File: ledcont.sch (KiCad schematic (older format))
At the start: 21 parts, among them J1 Screw_Terminal_01x02, J2 Screw_Terminal_01x02, Q1 ?, SW1 SW_SPST, U1 PAM2804

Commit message: Updated to the latest and greatest.
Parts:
- removed C?: 10uF, symbol Device:C
- removed D1, D2: TL431, symbol ledcont:TL431
- removed D3: LED, symbol Device:LED_Series
- removed Q1: ?, symbol Device:Q_PMOS_DGS
- removed R4: 1k, symbol Device:R
- removed R5: ?, symbol Device:R
- removed RV1: 5k, symbol Device:R_POT_TRIM
- removed RV2: ?, symbol Device:R_POT
- removed SW1: SW_SPST, symbol Switch:SW_SPST
- added C3: 10uF, Capacitor_SMD:C_1206_3216Metric, symbol Device:C
- added C4: 1uF, Capacitor_SMD:C_1206_3216Metric, symbol Device:C
- added C5, C6: .1uF, Capacitor_SMD:C_1206_3216Metric, symbol Device:C
- added D1: D_Schottky, symbol Device:D_Schottky
- added R10: 10k, Resistor_SMD:R_1206_3216Metric, symbol Device:R
- added R6: 1k, Resistor_SMD:R_1206_3216Metric, symbol Device:R
- added R7: 20k, Resistor_SMD:R_1206_3216Metric, symbol Device:R
- added R9: 9k, Resistor_SMD:R_1206_3216Metric, symbol Device:R
- added RV1: SPST, symbol ledcont:R_POT_SPST
- added U2: TSM102A, Package_SO:SOIC-16_3.9x9.9mm_P1.27mm, symbol Power_Management:TSM102A
- C1, C2: footprint (none) -> Capacitor_SMD:C_1206_3216Metric
- R1: value 10k -> 1k; footprint (none) -> Resistor_SMD:R_1206_3216Metric
- R2: value 1k -> 2k; footprint (none) -> Resistor_SMD:R_1206_3216Metric
- R3: footprint (none) -> Resistor_SMD:R_1206_3216Metric
- R4: renamed from R6; footprint (none) -> Resistor_SMD:R_1206_3216Metric
- R5: renamed from R7; footprint (none) -> Resistor_SMD:R_1206_3216Metric
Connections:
- net GND: now also R3.1, C3.2, C4.2, C5.2, C6.2, R10.2, RV1.1, RV1.2 (B), U2.13 (V-), U2.14 (+); no longer R1.2, R3.2
- net at R4.1, U1.5 (FB): now also R9.2
- net at C1.1, U1.4 (VIN): now also C3.1, C4.1, C5.1, D1.1 (K), RV1.5
- net at U1.1 (EN): now also R10.1, R6.2, U2.1; no longer R3.1
- net at R2.1: now also R3.2, U2.8
- net Vref: now reaches R1.1
- net Vref: now also R2.2, R7.1, U2.15 (-), U2.2 (-), U2.9
- net +BATT: no longer names the net of J1.1 (Pin_1)
- net +BATT: now also D1.2 (A); no longer R2.2
- new net: R7.2, RV1.3, U2.12 (+), U2.5 (+)
- new net: C6.1, R1.2, R6.1, RV1.4, U2.3 (+), U2.4 (V+)
- new net: R9.1, U2.6 (-), U2.7
- new net: U2.10 (-), U2.11
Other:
- note added: "18650 Battery"
- note added: "Unused"
- note added: "XXX -\nLet's always drive the output low? Is this right?"
- moved on the sheet: C1, C2, J1, J2, L1, R4, R5, U1

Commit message: Assigned footprints.
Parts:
- C1, C2, C3, C4, C5, C6: footprint Capacitor_SMD:C_1206_3216Metric -> Capacitor_SMD:C_1206_3216Metric_Pad1.42x1.75mm_HandSolder
- D1: footprint (none) -> Diode_SMD:D_1206_3216Metric_Pad1.42x1.75mm_HandSolder
- J1, J2: footprint (none) -> TerminalBlock_Phoenix:TerminalBlock_Phoenix_PT-1,5-2-3.5-H_1x02_P3.50mm_Horizontal
- L1: footprint (none) -> Inductor_SMD:L_1812_4532Metric_Pad1.30x3.40mm_HandSolder
- R1, R10, R2, R3, R4, R5, R6, R7, R9: footprint Resistor_SMD:R_1206_3216Metric -> Resistor_SMD:R_1206_3216Metric_Pad1.42x1.75mm_HandSolder
- RV1: footprint (none) -> ledcont:P091_S
- U1: footprint (none) -> ledcont:TSOT25
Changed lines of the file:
@@
 F 0 "R4" V 8107 3050 50  0000 C CNN
 F 1 "1k" V 8016 3050 50  0000 C CNN
-F 2 "Resistor_SMD:R_1206_3216Metric" V 7830 3050 50  0001 C CNN
+F 2 "Resistor_SMD:R_1206_3216Metric_Pad1.42x1.75mm_HandSolder" V 7830 3050 50  0001 C CNN
 F 3 "~" H 7900 3050 50  0001 C CNN
 	1    7900 3050
@@
 F 0 "R5" H 8630 3346 50  0000 R CNN
 F 1 "0.214" H 8630 3255 50  0000 R CNN
-F 2 "Resistor_SMD:R_1206_3216Metric" V 8630 3300 50  0001 C CNN
+F 2 "Resistor_SMD:R_1206_3216Metric_Pad1.42x1.75mm_HandSolder" V 8630 3300 50  0001 C CNN
 F 3 "~" H 8700 3300 50  0001 C CNN
 	1    8700 3300
@@
 F 0 "C2" H 8265 2396 50  0000 L CNN
 F 1 "10uF" H 8265 2305 50  0000 L CNN
-F 2 "Capacitor_SMD:C_1206_3216Metric" H 8188 2200 50  0001 C CNN
+F 2 "Capacitor_SMD:C_1206_3216Metric_Pad1.42x1.75mm_HandSolder" H 8188 2200 50  0001 C CNN
 F 3 "~" H 8150 2350 50  0001 C CNN
 	1    8150 2350
@@
 F 0 "L1" V 8040 2100 50  0000 C CNN
 F 1 "4.7uH" V 7949 2100 50  0000 C CNN
-F 2 "" H 7850 2100 50  0001 C CNN
+F 2 "Inductor_SMD:L_1812_4532Metric_Pad1.30x3.40mm_HandSolder" H 7850 2100 50  0001 C CNN
 F 3 "~" H 7850 2100 50  0001 C CNN
 	1    7850 2100
@@
 F 0 "U1" H 6550 2665 50  0000 C CNN
 F 1 "PAM2804" H 6550 2574 50  0000 C CNN
-F 2 "" H 6550 2250 50  0001 C CNN
+F 2 "ledcont:TSOT25" H 6550 2250 50  0001 C CNN
 F 3 "" H 6550 2250 50  0001 C CNN
 	1    6550 2250
@@
 F 0 "C1" H 5786 2396 50  0000 R CNN
 F 1 "10uF" H 5786 2305 50  0000 R CNN
-F 2 "Capacitor_SMD:C_1206_3216Metric" H 5938 2200 50  0001 C CNN
+F 2 "Capacitor_SMD:C_1206_3216Metric_Pad1.42x1.75mm_HandSolder" H 5938 2200 50  0001 C CNN
 F 3 "~" H 5900 2350 50  0001 C CNN
 	1    5900 2350
@@
 F 0 "J2" H 8980 2046 50  0000 L CNN
 F 1 "Screw_Terminal_01x02" H 8980 2001 50  0001 L CNN
-F 2 "" H 8900 2100 50  0001 C CNN
+F 2 "TerminalBlock_Phoenix:TerminalBlock_Phoenix_PT-1,5-2-3.5-H_1x02_P3.50mm_Horizontal" H 8900 2100 50  0001 C CNN
 F 3 "~" H 8900 2100 50  0001 C CNN
 	1    8900 2100
@@
 F 0 "J1" H 2670 2225 50  0000 C CNN
 F 1 "Screw_Terminal_01x02" H 2670 2226 50  0001 C CNN
-F 2 "" H 2750 2100 50  0001 C CNN
+F 2 "TerminalBlock_Phoenix:TerminalBlock_Phoenix_PT-1,5-2-3.5-H_1x02_P3.50mm_Horizontal" H 2750 2100 50  0001 C CNN
 F 3 "~" H 2750 2100 50  0001 C CNN
 	1    2750 2100
@@
 F 0 "RV1" H 6680 4246 50  0000 R CNN
 F 1 "SPST" H 6680 4155 50  0000 R CNN
-F 2 "" H 6750 4200 50  0001 C CNN
+F 2 "ledcont:P091_S" H 6750 4200 50  0001 C CNN
 F 3 "~" H 6750 4200 50  0001 C CNN
 	1    6750 4200
@@
 F 0 "RV1" H 5088 2396 50  0000 L CNN
 F 1 "SPST" H 5088 2305 50  0001 L CNN
-F 2 "" H 4950 2350 50  0001 C CNN
+F 2 "ledcont:P091_S" H 4950 2350 50  0001 C CNN
 F 3 "~" H 4950 2350 50  0001 C CNN
 	2    4950 2350
@@
 F 0 "R1" V 4243 3500 50  0000 C CNN
 F 1 "1k" V 4334 3500 50  0000 C CNN
-F 2 "Resistor_SMD:R_1206_3216Metric" V 4380 3500 50  0001 C CNN
+F 2 "Resistor_SMD:R_1206_3216Metric_Pad1.42x1.75mm_HandSolder" V 4380 3500 50  0001 C CNN
 F 3 "~" H 4450 3500 50  0001 C CNN
 	1    4450 3500
@@
 F 0 "R2" H 4130 4104 50  0000 R CNN
 F 1 "2k" H 4130 4195 50  0000 R CNN
-F 2 "Resistor_SMD:R_1206_3216Metric" V 4130 4150 50  0001 C CNN
+F 2 "Resistor_SMD:R_1206_3216Metric_Pad1.42x1.75mm_HandSolder" V 4130 4150 50  0001 C CNN
 F 3 "~" H 4200 4150 50  0001 C CNN
 	1    4200 4150
@@
 F 0 "R3" H 4130 4504 50  0000 R CNN
 F 1 "10k" H 4130 4595 50  0000 R CNN
-F 2 "Resistor_SMD:R_1206_3216Metric" V 4130 4550 50  0001 C CNN
+F 2 "Resistor_SMD:R_1206_3216Metric_Pad1.42x1.75mm_HandSolder" V 4130 4550 50  0001 C CNN
 F 3 "~" H 4200 4550 50  0001 C CNN
 	1    4200 4550
@@
 F 0 "R6" V 5757 3050 50  0000 C CNN
 F 1 "1k" V 5666 3050 50  0000 C CNN
-F 2 "Resistor_SMD:R_1206_3216Metric" V 5480 3050 50  0001 C CNN
+F 2 "Resistor_SMD:R_1206_3216Metric_Pad1.42x1.75mm_HandSolder" V 5480 3050 50  0001 C CNN
 F 3 "~" H 5550 3050 50  0001 C CNN
 	1    5550 3050
@@
 F 0 "R7" H 6820 3846 50  0000 L CNN
 F 1 "20k" H 6820 3755 50  0000 L CNN
-F 2 "Resistor_SMD:R_1206_3216Metric" V 6680 3800 50  0001 C CNN
+F 2 "Resistor_SMD:R_1206_3216Metric_Pad1.42x1.75mm_HandSolder" V 6680 3800 50  0001 C CNN
 F 3 "~" H 6750 3800 50  0001 C CNN
 	1    6750 3800
@@
 F 0 "R9" V 7607 3050 50  0000 C CNN
 F 1 "9k" V 7516 3050 50  0000 C CNN
-F 2 "Resistor_SMD:R_1206_3216Metric" V 7330 3050 50  0001 C CNN
+F 2 "Resistor_SMD:R_1206_3216Metric_Pad1.42x1.75mm_HandSolder" V 7330 3050 50  0001 C CNN
 F 3 "~" H 7400 3050 50  0001 C CNN
 	1    7400 3050
@@
 F 0 "D1" H 3400 1884 50  0000 C CNN
 F 1 "D_Schottky" H 3400 1975 50  0000 C CNN
-F 2 "" H 3400 2100 50  0001 C CNN
+F 2 "Diode_SMD:D_1206_3216Metric_Pad1.42x1.75mm_HandSolder" H 3400 2100 50  0001 C CNN
 F 3 "~" H 3400 2100 50  0001 C CNN
 	1    3400 2100
@@
 F 0 "C3" H 3636 2296 50  0000 R CNN
 F 1 "10uF" H 3636 2205 50  0000 R CNN
-F 2 "Capacitor_SMD:C_1206_3216Metric" H 3788 2100 50  0001 C CNN
+F 2 "Capacitor_SMD:C_1206_3216Metric_Pad1.42x1.75mm_HandSolder" H 3788 2100 50  0001 C CNN
 F 3 "~" H 3750 2250 50  0001 C CNN
 	1    3750 2250
@@
 F 0 "C4" H 4036 2296 50  0000 R CNN
 F 1 "1uF" H 4036 2205 50  0000 R CNN
-F 2 "Capacitor_SMD:C_1206_3216Metric" H 4188 2100 50  0001 C CNN
+F 2 "Capacitor_SMD:C_1206_3216Metric_Pad1.42x1.75mm_HandSolder" H 4188 2100 50  0001 C CNN
 F 3 "~" H 4150 2250 50  0001 C CNN
 	1    4150 2250
@@
 F 0 "C5" H 4486 2296 50  0000 R CNN
 F 1 ".1uF" H 4486 2205 50  0000 R CNN
-F 2 "Capacitor_SMD:C_1206_3216Metric" H 4638 2100 50  0001 C CNN
+F 2 "Capacitor_SMD:C_1206_3216Metric_Pad1.42x1.75mm_HandSolder" H 4638 2100 50  0001 C CNN
 F 3 "~" H 4600 2250 50  0001 C CNN
 	1    4600 2250
@@
 F 0 "R10" H 6170 3646 50  0000 L CNN
 F 1 "10k" H 6170 3555 50  0000 L CNN
-F 2 "Resistor_SMD:R_1206_3216Metric" V 6030 3600 50  0001 C CNN
+F 2 "Resistor_SMD:R_1206_3216Metric_Pad1.42x1.75mm_HandSolder" V 6030 3600 50  0001 C CNN
 F 3 "~" H 6100 3600 50  0001 C CNN
 	1    6100 3600
@@
 F 0 "C6" H 5065 3996 50  0000 L CNN
 F 1 ".1uF" H 5065 3905 50  0000 L CNN
-F 2 "Capacitor_SMD:C_1206_3216Metric" H 4988 3800 50  0001 C CNN
+F 2 "Capacitor_SMD:C_1206_3216Metric_Pad1.42x1.75mm_HandSolder" H 4988 3800 50  0001 C CNN
 F 3 "~" H 4950 3950 50  0001 C CNN
 	1    4950 3950

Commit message: More progress.
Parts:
- C1: renamed from C3; Part (none) -> CL31B106KOHNFNE
- C2: renamed from C4; Part (none) -> CL31B105MAHNNNE
- C3: renamed from C5; Part (none) -> CL31B104KBCNNNC
- C4: renamed from C6; Part (none) -> CL31B104KBCNNNC
- C5: renamed from C1; Part (none) -> CL31B106KOHNFNE
- C6: renamed from C2; Part (none) -> CL31B106KOHNFNE
- D1: footprint Diode_SMD:D_1206_3216Metric_Pad1.42x1.75mm_HandSolder -> Diode_SMD:D_SOD-123F; Part (none) -> NRVTS245ESFT1G
- J1, J2: Part (none) -> 1984617
- L1: Part (none) -> LQH43PN4R7M26L
- R1: renamed from R2; Part (none) -> RC1206FR-072KL; Tolerance (none) -> 1%
- R2: renamed from R3; Part (none) -> RC1206FR-0710KL; Tolerance (none) -> 1%
- R3: renamed from R1; Part (none) -> RC1206FR-071KL; Tolerance (none) -> 1%
- R4: renamed from R6; Part (none) -> RC1206FR-071KL; Tolerance (none) -> 1%
- R5: renamed from R10; Part (none) -> RC1206FR-0710KL; Tolerance (none) -> 1%
- R6: renamed from R7; Part (none) -> RC1206FR-0720KL
- R7: renamed from R9; Part (none) -> RC1206FR-079K09L; Tolerance (none) -> 1%
- R8: renamed from R4; Part (none) -> RC1206FR-071KL; Tolerance (none) -> 1%
- R9: renamed from R5; value 0.214 -> 0.200; Part (none) -> PT1206FR-070R2L; Tolerance (none) -> 1%
- RV1: Part (none) -> P091S-FC20BR10K
- U1: Part (none) -> PAM2804AAB010
- U2: Part (none) -> TSM102AIDT

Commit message: Checkpoint before real board layout.
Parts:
- RV1: value SPST -> 10k
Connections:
- net GND: now also RV1.3; no longer RV1.1
- net at R6.2, U2.12 (+), U2.5 (+): now also RV1.1; no longer RV1.3
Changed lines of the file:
@@
 U 1 1 5C458CC6
 P 6750 4200
-F 0 "RV1" H 6680 4246 50  0000 R CNN
-F 1 "SPST" H 6680 4155 50  0000 R CNN
+F 0 "RV1" H 6680 4154 50  0000 R CNN
+F 1 "10k" H 6680 4245 50  0000 R CNN
 F 2 "ledcont:P091_S" H 6750 4200 50  0001 C CNN
 F 3 "~" H 6750 4200 50  0001 C CNN
 F 4 "P091S-FC20BR10K" H 0   0   50  0001 C CNN "Part"
 	1    6750 4200
-	-1   0    0    -1
+	-1   0    0    1
 $EndComp
 $Comp

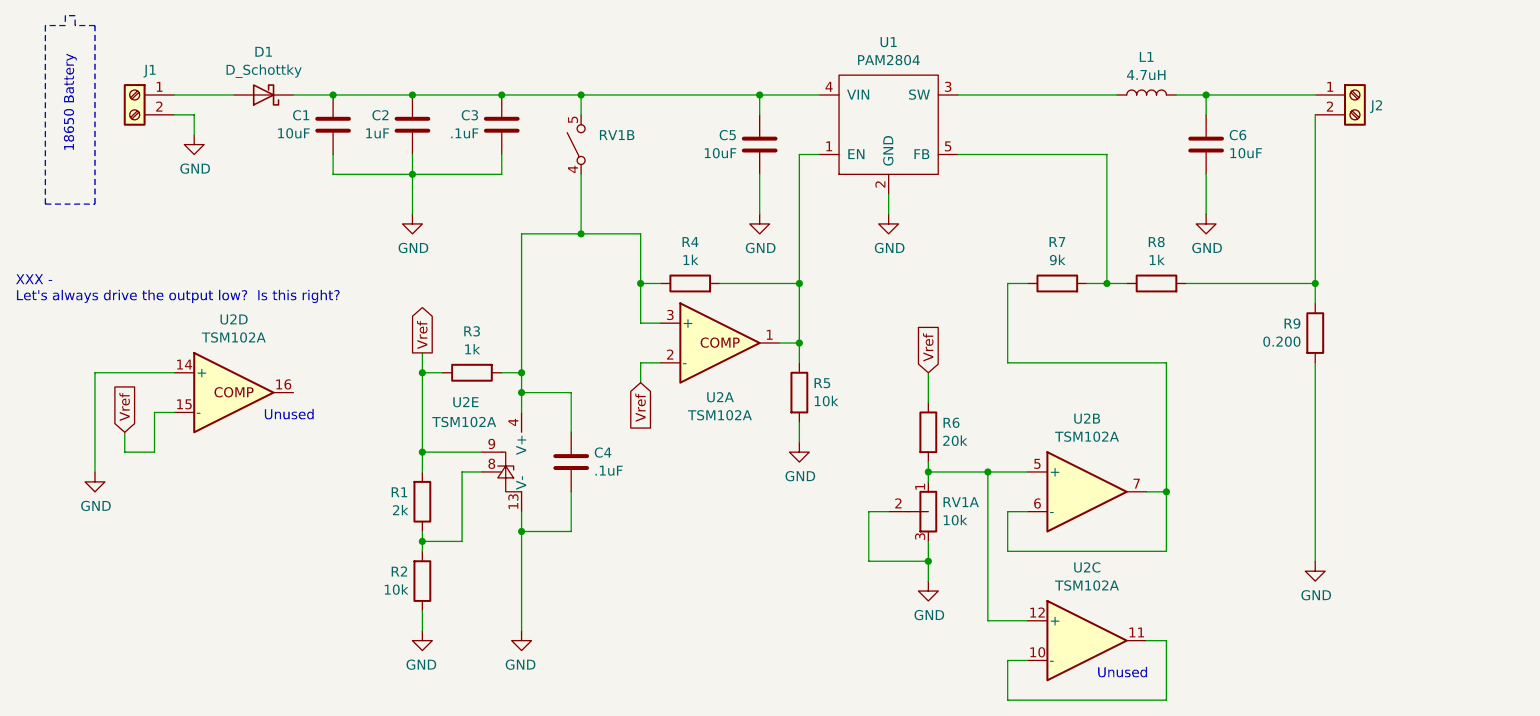
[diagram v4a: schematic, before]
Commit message: Finished first attempt at board layout.
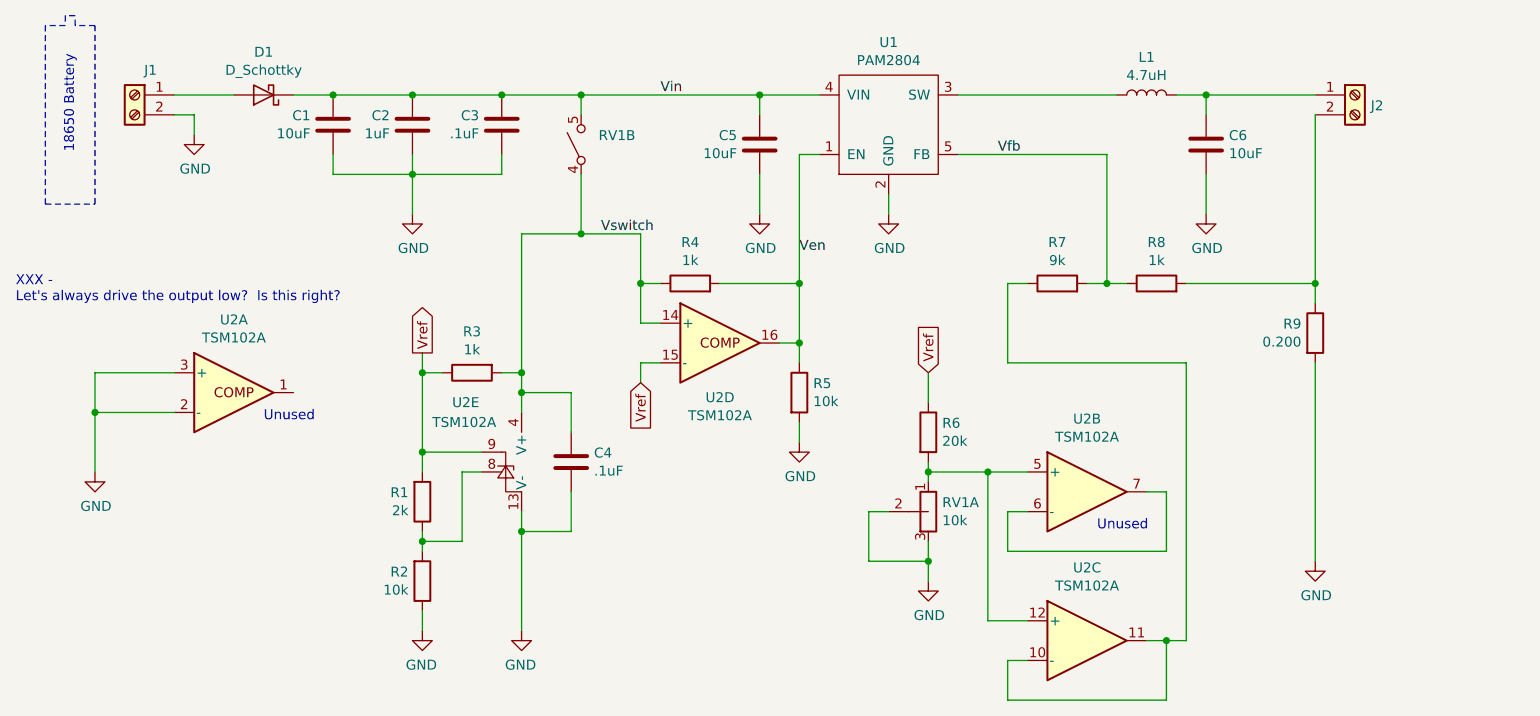
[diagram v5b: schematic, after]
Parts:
- RV1: value SPST -> 10k
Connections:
- net GND: now also U2.2 (-), U2.3 (+); no longer U2.14 (+)
- net Vref: now also U2.15 (-); no longer U2.15 (-), U2.2 (-)
- net Vfb: now reaches R7.2, R8.1, U1.5 (FB)
- net Vin: now reaches C1.1, C2.1, C3.1, C5.1, D1.1 (K), RV1.5, U1.4 (VIN)
- net Vswitch: now reaches C4.1, R3.2, R4.1, RV1.4, U2.4 (V+)
- net Vswitch: now also U2.14 (+); no longer U2.3 (+)
- net Ven: now reaches R4.2, R5.1, U1.1 (EN)
- net Ven: now also U2.16; no longer U2.1
- net at U2.6 (-), U2.7: no longer R7.1
- net at U2.10 (-), U2.11: now also R7.1
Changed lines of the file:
@@
 P 4950 2350
 F 0 "RV1" H 5088 2396 50  0000 L CNN
-F 1 "SPST" H 5088 2305 50  0001 L CNN
+F 1 "10k" H 5088 2305 50  0001 L CNN
 F 2 "ledcont:P091_S" H 4950 2350 50  0001 C CNN
 F 3 "~" H 4950 2350 50  0001 C CNN
@@
 $Comp
 L Power_Management:TSM102A U2
-U 1 1 5C4640C2
+U 4 1 5C4640C2
 P 5700 3350
 F 0 "U2" H 5700 3075 50  0000 C CNN
@@
 F 3 "http://www.st.com/resource/en/datasheet/tsm102.pdf" H 5750 3550 50  0001 C CNN
 F 4 "TSM102AIDT" H 0   0   50  0001 C CNN "Part"
-	1    5700 3350
+	4    5700 3350
 	1    0    0    -1
 $EndComp
@@
 Wire Wire Line
 	7150 4200 7150 4400
-Wire Wire Line
-	7150 4400 7950 4400
-Wire Wire Line
-	7950 4400 7950 4100
 $Comp
 L Device:R R7
@@
 Wire Wire Line
 	7950 4850 7850 4850
-Text Notes 7600 5050 0    50   ~ 0
+Text Notes 7600 4300 0    50   ~ 0
 Unused
 Text Notes 3400 3750 0    50   ~ 0
@@
 $Comp
 L Power_Management:TSM102A U2
-U 4 1 5C4AD8B0
+U 1 1 5C4AD8B0
 P 3250 3600
 F 0 "U2" H 3250 3967 50  0000 C CNN
@@
 F 3 "http://www.st.com/resource/en/datasheet/tsm102.pdf" H 3300 3800 50  0001 C CNN
 F 4 "TSM102AIDT" H 0   0   50  0001 C CNN "Part"
-	4    3250 3600
+	1    3250 3600
 	1    0    0    -1
 $EndComp
 Wire Wire Line
 	2950 3500 2550 3500
-Text GLabel 2700 3800 1    50   Input ~ 0
-Vref
-Wire Wire Line
-	2550 3500 2550 4000
-Wire Wire Line
-	2850 3900 2700 3900
-Wire Wire Line
-	2700 3900 2700 3800
-Wire Wire Line
-	2950 3700 2850 3700
-Wire Wire Line
-	2850 3700 2850 3900
+Wire Wire Line
+	2550 3500 2550 3700
 Text Notes 2150 3150 0    50   ~ 0
 XXX -\nLet's always drive the output low?  Is this right?
@@
 	6100 3750 6100 3850
 Connection ~ 7050 4000
-Connection ~ 7950 4100
 Wire Wire Line
 	7950 4100 7850 4100
@@
 Wire Wire Line
 	7150 3050 7150 3450
-Wire Wire Line
-	7150 3450 7950 3450
-Wire Wire Line
-	7950 3450 7950 4100
 Text GLabel 5300 3550 3    50   Input ~ 0
 Vref
@@
 	1    0    0    -1
 $EndComp
+Text Label 5100 2800 0    50   ~ 0
+Vswitch
+Text Label 5400 2100 0    50   ~ 0
+Vin
+Text Label 7100 2400 0    50   ~ 0
+Vfb
+Wire Wire Line
+	7150 4400 7950 4400
+Wire Wire Line
+	7950 4100 7950 4400
+Wire Wire Line
+	8050 3450 8050 4850
+Wire Wire Line
+	8050 4850 7950 4850
+Wire Wire Line
+	7150 3450 8050 3450
+Connection ~ 7950 4850
+Text Label 6100 2900 0    50   ~ 0
+Ven
+Wire Wire Line
+	2950 3700 2550 3700
+Connection ~ 2550 3700
+Wire Wire Line
+	2550 3700 2550 4000
 $EndSCHEMATC

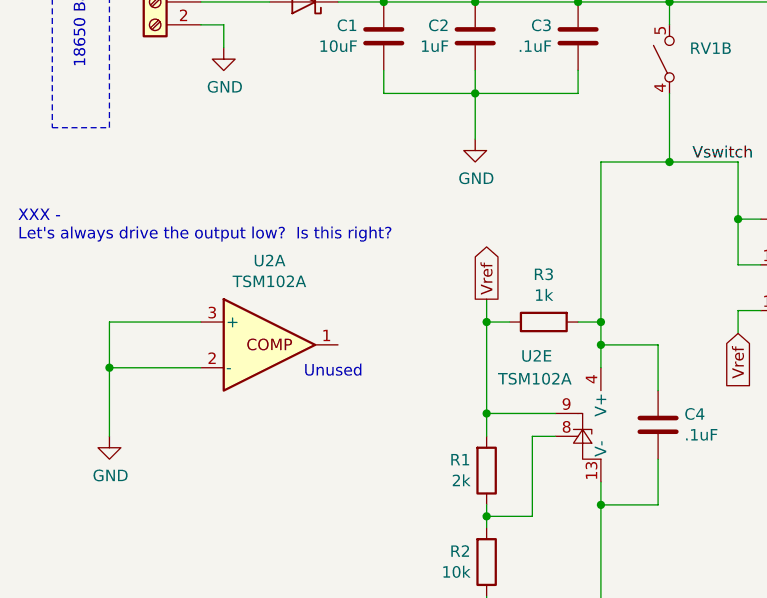
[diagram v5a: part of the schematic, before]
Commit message: Board cutout.  Rewired unused comparator.
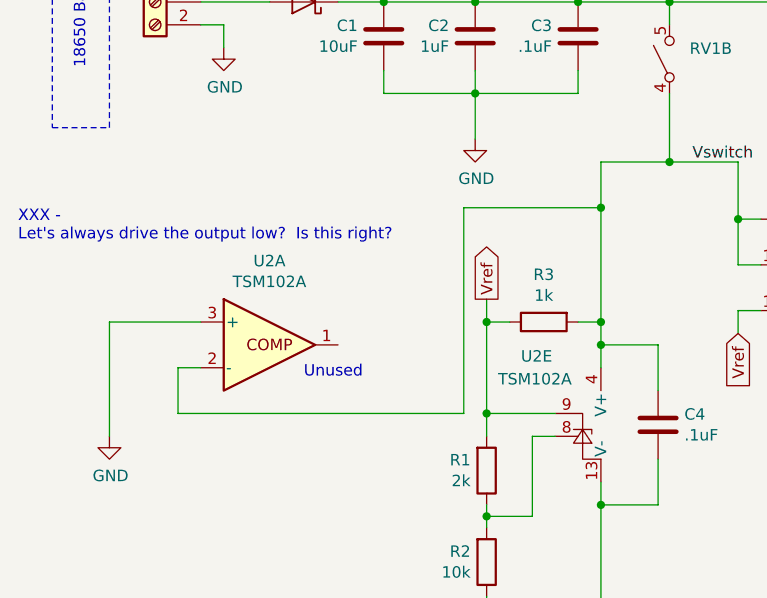
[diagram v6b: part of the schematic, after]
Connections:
- net GND: no longer U2.2 (-)
- net Vswitch: now also U2.2 (-)
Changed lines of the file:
@@
 Wire Wire Line
 	2950 3500 2550 3500
-Wire Wire Line
-	2550 3500 2550 3700
 Text Notes 2150 3150 0    50   ~ 0
 XXX -\nLet's always drive the output low?  Is this right?
@@
 	5300 3450 5300 3550
 Wire Wire Line
-	4700 2800 4700 3500
+	4700 2800 4700 3000
 Connection ~ 5000 2800
 Connection ~ 4700 3500
@@
 Ven
 Wire Wire Line
-	2950 3700 2550 3700
-Connection ~ 2550 3700
-Wire Wire Line
-	2550 3700 2550 4000
+	2550 3500 2550 4000
+Wire Wire Line
+	2950 3700 2850 3700
+Wire Wire Line
+	2850 3700 2850 3900
+Wire Wire Line
+	2850 3900 4100 3900
+Wire Wire Line
+	4100 3900 4100 3000
+Wire Wire Line
+	4100 3000 4700 3000
+Connection ~ 4700 3000
+Wire Wire Line
+	4700 3000 4700 3500
 $EndSCHEMATC
